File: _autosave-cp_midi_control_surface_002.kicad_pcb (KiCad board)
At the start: 2 copper layers, 421.6 x 332.7 mm, 174 parts, among them J1 Conn_02x05_Odd_Even, J2 Conn_02x05_Odd_Even, J7 Conn_02x05_Odd_Even, P1 Power, P11 Guide, P12 Guide, P13 Guide, P2 Analogue, P3 Digital, P4 Communication, P5 PWM, P6 PWM, P8 Guide, P9 Guide, SW1 B3F-5050, SW10 B3F-5050, SW11 B3F-5050, SW12 B3F-5050, SW13 B3F-5050, SW14 B3F-5050, SW15 B3F-5050, SW16 B3F-5050, SW17 B3F-5050, SW18 B3F-5050, SW19 B3F-5050, SW2 B3F-5050, SW20 B3F-5050, SW21 B3F-5050, SW22 B3F-5050, SW23 B3F-5050, SW24 B3F-5050, SW25 B3F-5050, SW26 B3F-5050, SW27 B3F-5050, SW28 B3F-5050, SW29 B3F-5050, SW3 B3F-5050, SW30 B3F-5050, SW31 B3F-5050, SW32 B3F-5050, SW4 B3F-5050, SW41 B3F-5050, SW42 B3F-5050, SW43 B3F-5050, SW44 B3F-5050, SW45 B3F-5050, SW46 B3F-5050, SW47 B3F-5050, SW48 B3F-5050, SW49 B3F-5050, SW5 B3F-5050, SW50 B3F-5050, SW51 B3F-5050, SW52 B3F-5050, SW53 B3F-5050, SW54 B3F-5050, SW55 B3F-5050, SW56 B3F-5050, SW6 B3F-5050, SW7 B3F-5050, SW8 B3F-5050, SW9 B3F-5050, U1 CD74HC4067M, U2 CD74HC4067M, U3 CD74HC4067M, U4 CD74HC4067M, U5 CD74HC4067M, U6 CD74HC4067M

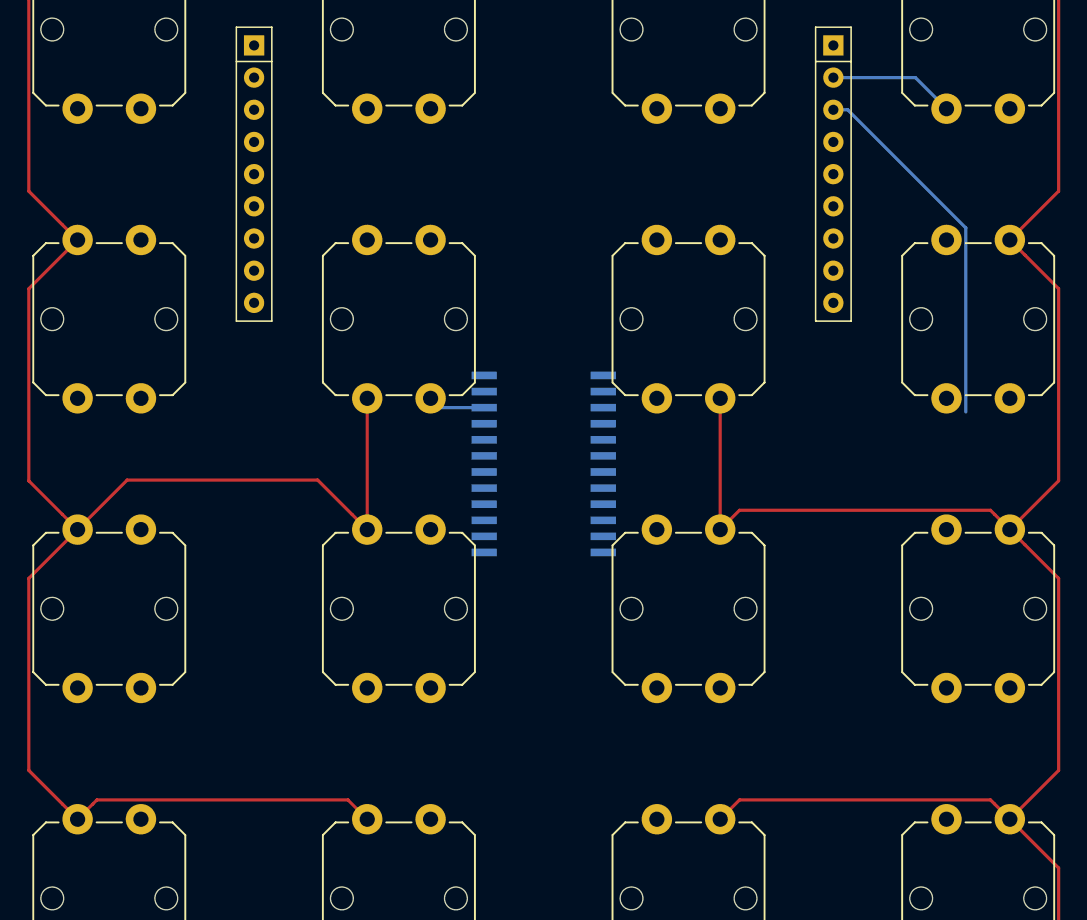
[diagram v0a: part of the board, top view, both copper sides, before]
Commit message: Routing left button blocks (traces for bottom buttons TBD)
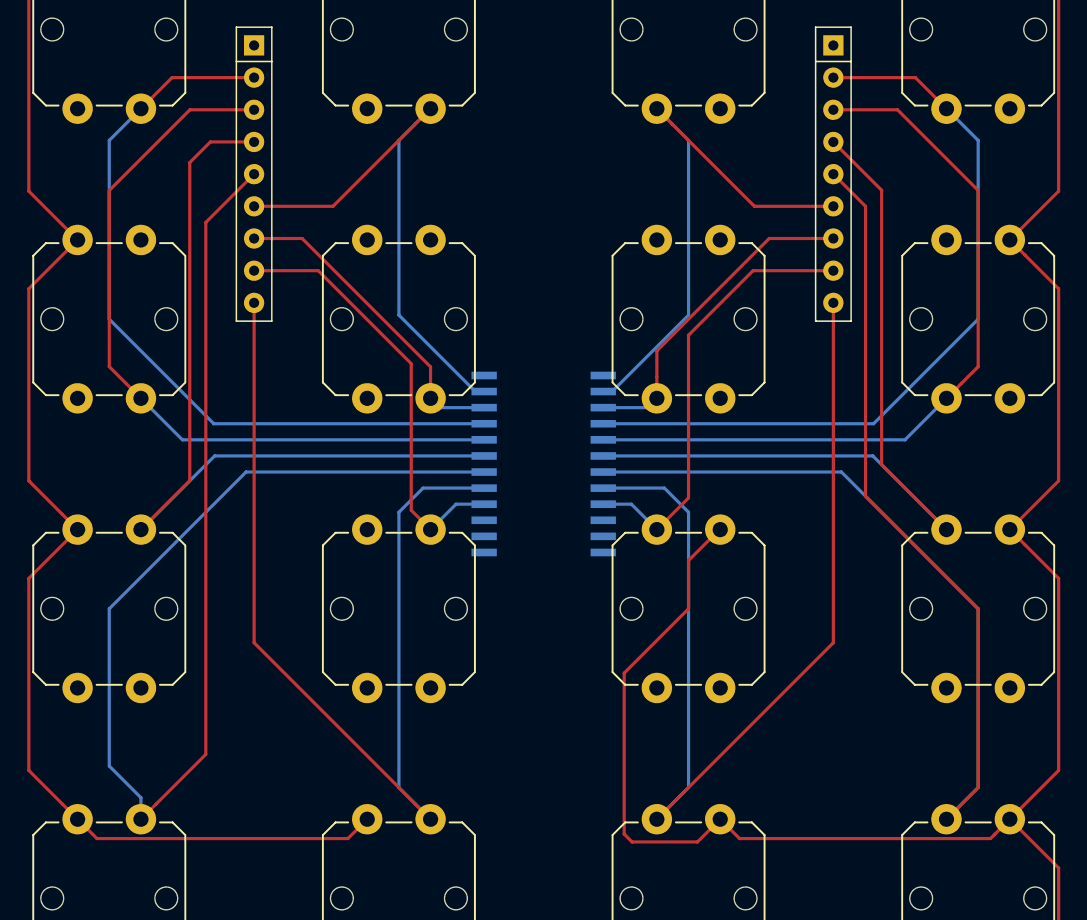
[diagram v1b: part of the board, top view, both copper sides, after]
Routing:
- net Net-(RN5-Pad5): track 0.00 -> 108.4 mm
- net Net-(RN4-Pad5): track 0.00 -> 106.3 mm
- net Net-(RN5-Pad9): track 0.00 -> 79.3 mm
- net Net-(RN4-Pad9): track 0.00 -> 79.3 mm
- net Net-(RN4-Pad4): track 0.00 -> 65.8 mm
- net Net-(RN5-Pad4): track 0.00 -> 63.8 mm
- net Net-(RN4-Pad2): track 0.00 -> 60.6 mm
- net Net-(RN4-Pad3): track 0.00 -> 60.0 mm
- net Net-(RN5-Pad2): track 9.95 -> 60.6 mm
- net Net-(RN5-Pad6): track 0.00 -> 43.7 mm
- net Net-(RN4-Pad6): track 0.00 -> 43.7 mm
- net +5V: track 1415.7 -> 1380.5 mm
- net Net-(RN5-Pad8): track 0.00 -> 35.0 mm
- net Net-(RN4-Pad8): track 0.00 -> 34.2 mm
- net Net-(RN5-Pad3): track 28.8 -> 60.0 mm
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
